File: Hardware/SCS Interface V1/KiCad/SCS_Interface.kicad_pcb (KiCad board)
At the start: 2 copper layers, 42 x 52.3 mm, 37 parts, among them J1 SCS, J2 Headder, Q1 MMBTA06, Q2 MMBTA06, U1 LMR51420, U2 AZ1117CH2 - 3.3

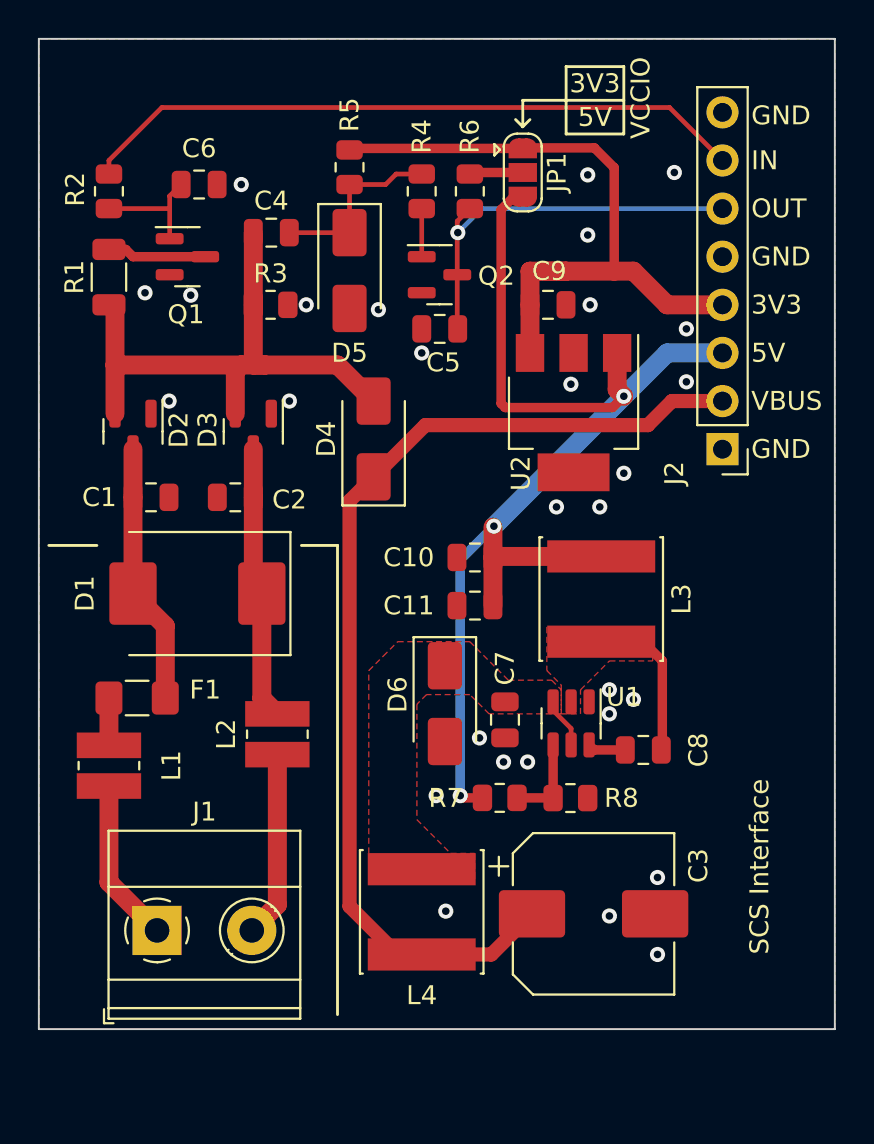
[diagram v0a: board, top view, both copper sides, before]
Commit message: Update PCB after first pcb build
- Replace input detection
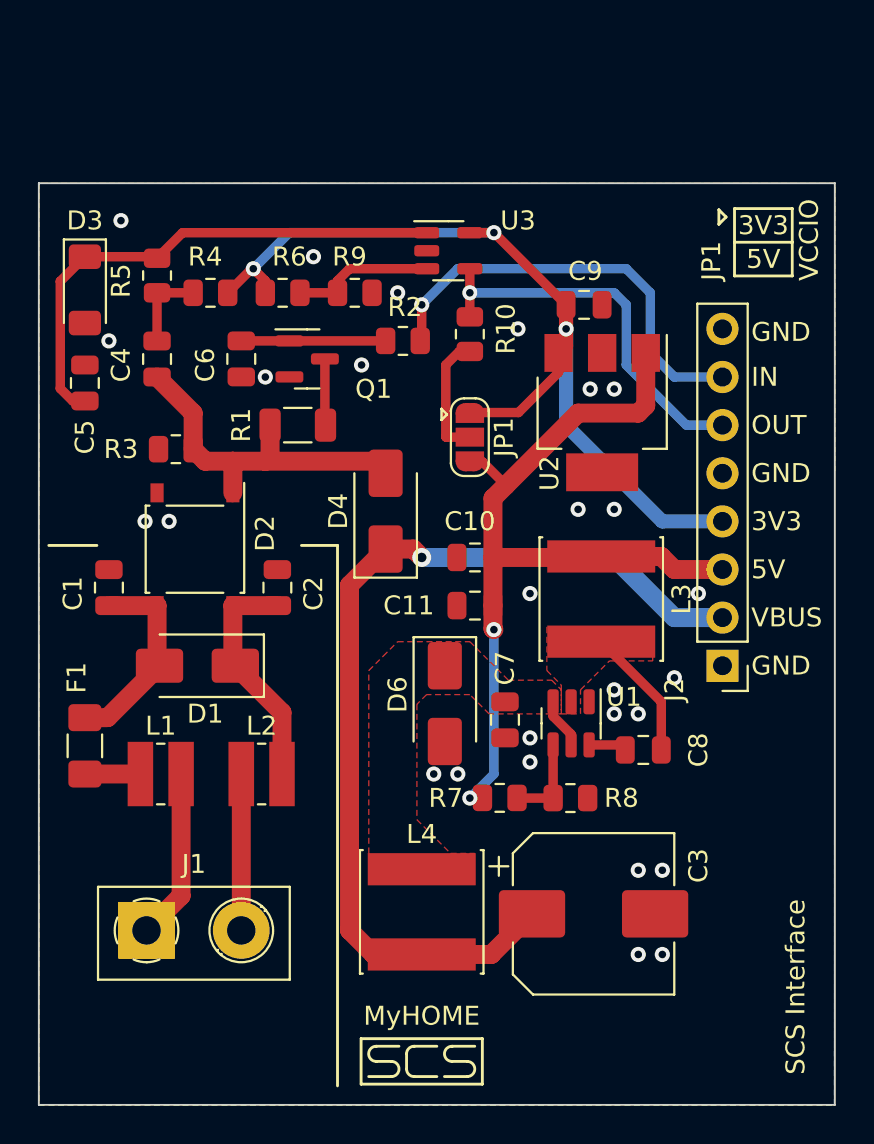
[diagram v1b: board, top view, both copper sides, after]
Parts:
- removed D5: M2, Diode_SMD:D_SMA
- removed Q2: MMBTA06, Package_TO_SOT_SMD:SOT-23
- added R10: 10k, Resistor_SMD:R_0805_2012Metric, F.Cu at (158.8, 66.3)
- added R9: 10k, Resistor_SMD:R_0805_2012Metric, F.Cu at (152.7, 64.1)
- added U3: LM397, Package_TO_SOT_SMD:SOT-23-5, F.Cu at (157.6, 61.9)
- C5: value 1n -> 13p (OPT)
- D1: value TPSMC33A -> P4SMA39CA; footprint Diode_SMD:D_SMC -> Diode_SMD:D_SMA
- D2: value BAS31 -> ABS2; footprint Package_TO_SOT_SMD:SOT-23 -> Diode_SMD:Diode_Bridge_Diotec_ABS
- D3: value BAS31 -> FDLL4148; footprint Package_TO_SOT_SMD:SOT-23 -> Diode_SMD:D_MiniMELF
- J1: footprint TerminalBlock_Phoenix:TerminalBlock_Phoenix_MKDS-1,5-2_1x02_P5.00mm_Horizontal -> TerminalBlock_Phoenix:TerminalBlock_Phoenix_MKDS-1,5-2_1x02_P5.00mm_Horizontal_PNP
- R4: value 100k -> 10k
- R6: value 10k -> 20k
- moved C5 18.9 mm to (138.4, 68.9), turned to -90 degrees
- moved R2 17.4 mm to (155.2, 66.7), turned to 180 degrees
- moved JP1 14.2 mm to (158.8, 71.8)
- moved R1 12.7 mm to (149.7, 71.1), turned to 0 degrees
- moved R4 12.4 mm to (145.1, 64.1), turned to 0 degrees
- moved R5 11.7 mm to (142.2, 63.2)
- moved D3 11.6 mm to (138.4, 64.0)
- moved J2 11.4 mm to (172.1, 83.8)
- moved R6 11.2 mm to (148.9, 64.1), turned to 180 degrees
- moved C6 9.47 mm to (146.7, 67.6), turned to 90 degrees
- moved R3 9.11 mm to (143.2, 72.4), turned to 180 degrees
- moved C4 8.99 mm to (142.2, 67.6), turned to 90 degrees
- moved Q1 8.31 mm to (150.2, 67.6)
- moved D2 7.02 mm to (144.2, 77.7)
- moved C1 5.26 mm to (139.7, 79.7), turned to 90 degrees
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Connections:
- C5 pad 2: SCS_OUT -> Net-(D3-K)
- D2 pad 1: GND -> SCS_BUS_CC
- D2 pad 2: SCS_BUS_CC -> GND
- D3 pad 1: GND -> Net-(D3-K)
- D3 pad 2: SCS_BUS_CC -> GND
- R4 pad 2: Net-(Q2-B) -> +3V3
- R5 pad 2: +3V3 -> Net-(D3-K)
- R6 pad 1: SCS_OUT -> Net-(U3-+)
- R6 pad 2: VCC_IO -> +3V3
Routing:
- net Net-(D3-K): track 0.00 -> 27.7 mm
- net +5V: track 62.8 -> 44.8 mm, vias 3 -> 2
- net SCS_IN: track 35.4 -> 22.8 mm, vias 0 -> 1
- net +3V3: track 36.4 -> 48.3 mm, vias 0 -> 3
- net SCS_BUS_CC: track 30.6 -> 19.0 mm
- net Net-(U3-+): track 0.00 -> 7.59 mm
- net Net-(C4-Pad2): track 9.76 -> 4.45 mm
- net VCC_IO: track 2.83 -> 6.63 mm
- net VBUS: track 54.8 -> 51.2 mm, vias 0 -> 1
- net Net-(D1-A2): track 13.8 -> 10.8 mm
- net Net-(Q2-B): track 2.54 -> 0.00 mm
- net Net-(D1-A1): track 14.5 -> 12.3 mm
- net Net-(Q1-C): track 5.24 -> 3.51 mm
- net Net-(J1-Pin_2): track 9.84 -> 8.26 mm
- net Net-(U1-SW): track 8.37 -> 7.03 mm
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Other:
- board size 42 x 52.3 mm -> 42 x 48.6 mm
- board text added: "JP1"
- board text added: "MyHOME"
